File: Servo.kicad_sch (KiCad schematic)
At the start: 80 parts, among them J2 Conn_01x03_Pin, J3 Conn_01x03_Pin, J31 Conn_01x03_Pin, J32 Conn_01x03_Pin, J33 Conn_01x03_Pin, J34 Conn_01x03_Pin, J35 Conn_01x03_Pin, J36 Conn_01x03_Pin, J37 Conn_01x03_Pin, J38 Conn_01x03_Pin, J4 Conn_01x03_Pin, J5 Conn_01x03_Pin, J6 Conn_01x03_Pin, J7 Conn_01x03_Pin, J8 Conn_01x03_Pin, J9 Conn_01x03_Pin, Q19 2N7002, Q20 2N7002, Q21 2N7002, Q22 2N7002, Q23 2N7002, Q24 2N7002, Q25 2N7002, Q26 2N7002, Q27 2N7002, Q28 2N7002, Q29 2N7002, Q30 2N7002, Q31 2N7002, Q32 2N7002, Q33 2N7002, Q34 2N7002

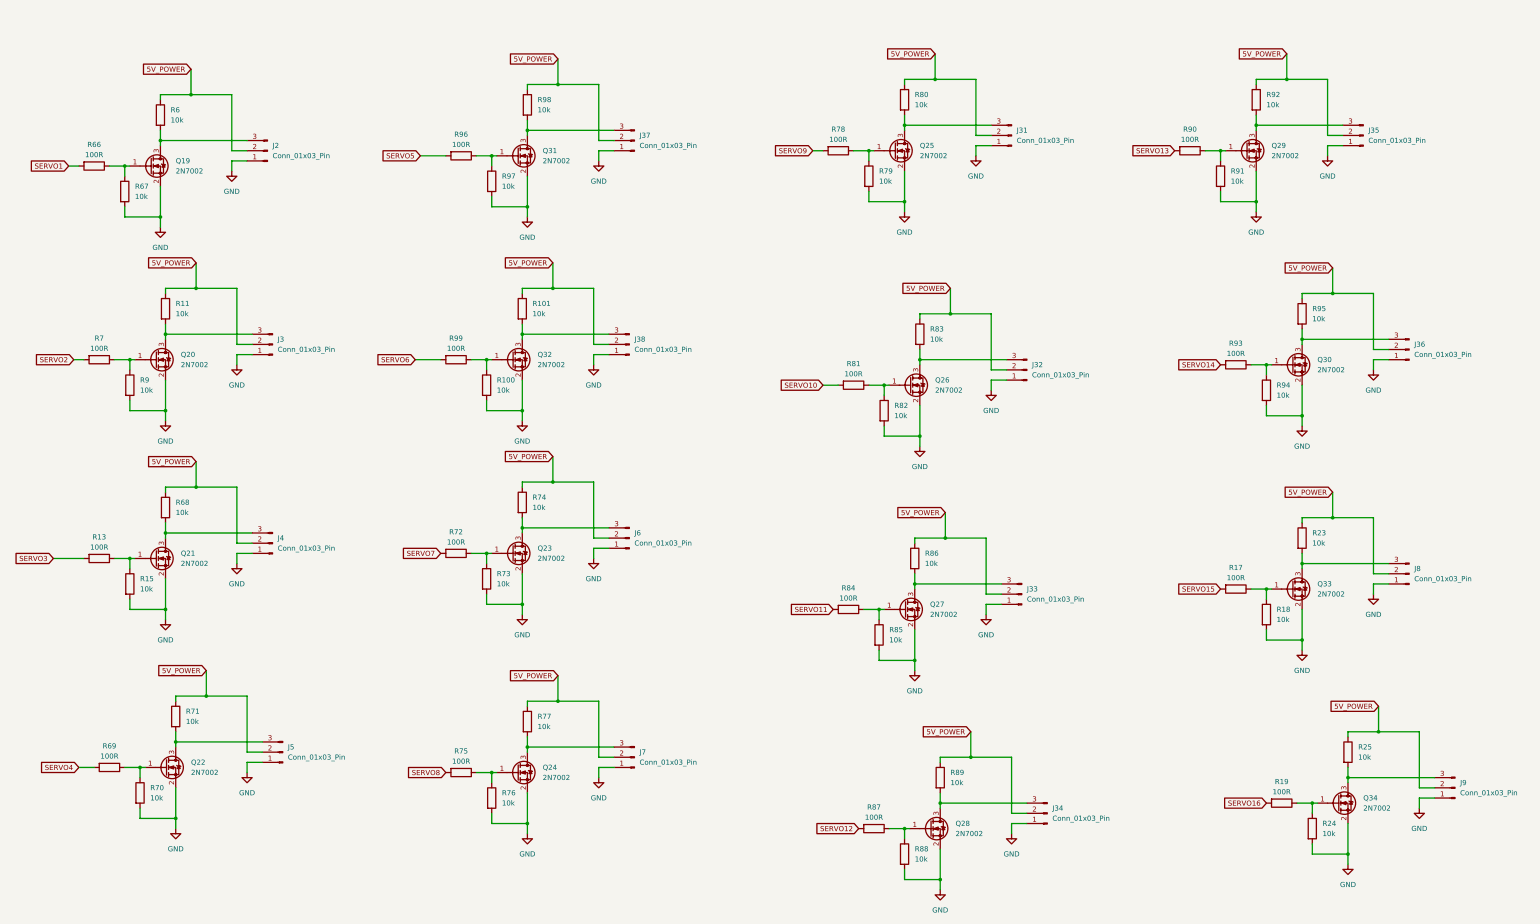
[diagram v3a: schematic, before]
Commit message: update schematic for feedback
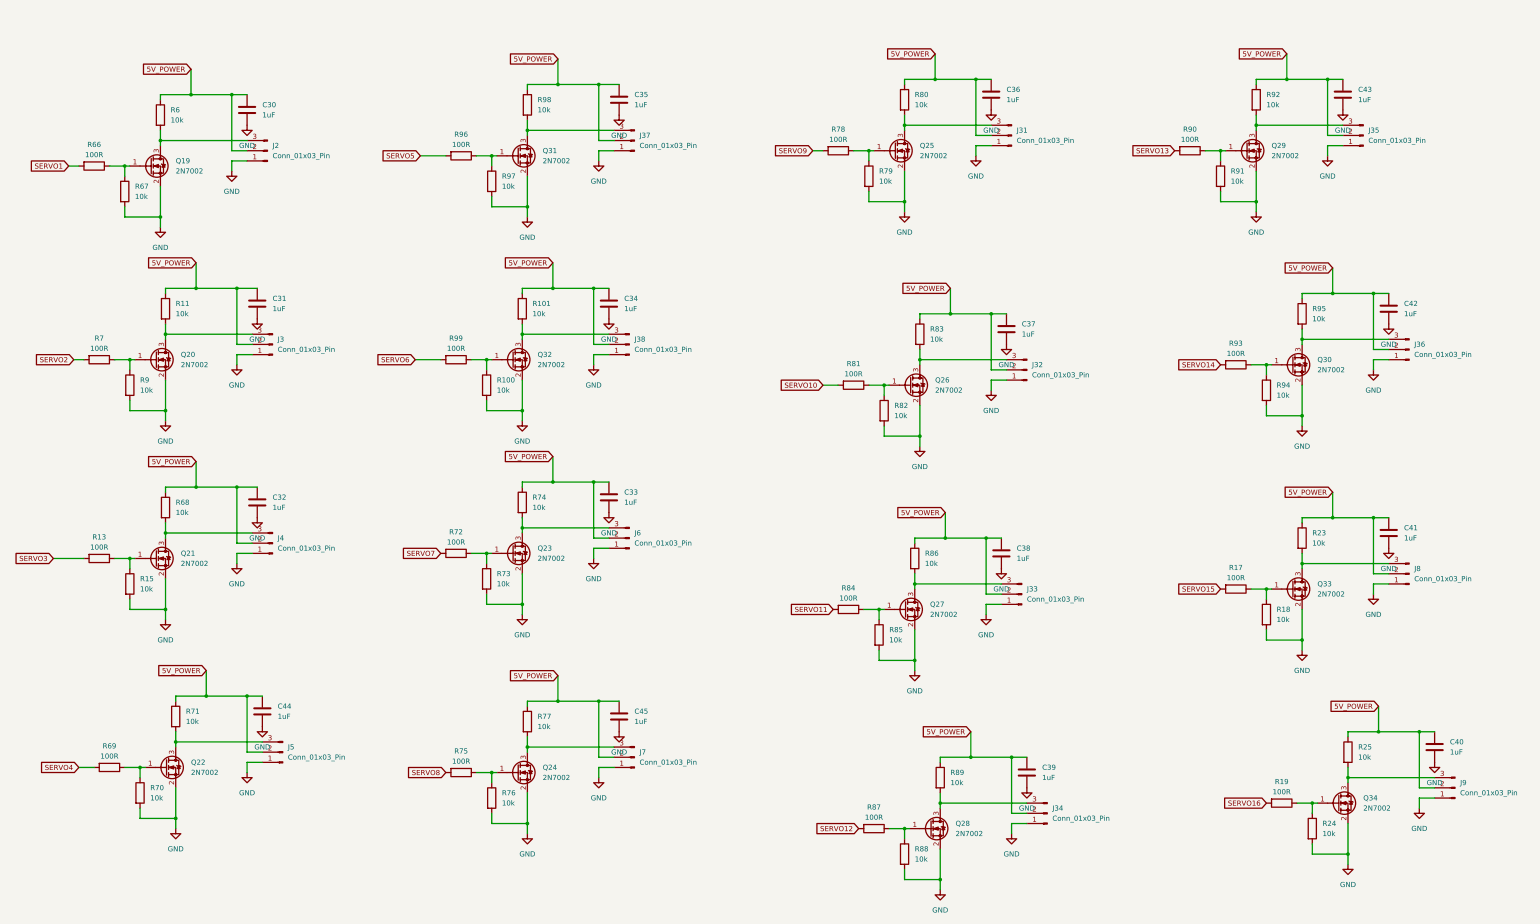
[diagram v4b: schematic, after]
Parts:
- added C30, C31, C32, C33, C34, C35, C36, C37, C38, C39, C40, C41, C42, C43, C44, C45: 1uF, Capacitor_SMD:C_0402_1005Metric, symbol Device:C
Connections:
- net 5V_POWER: now also C30.1, C31.1, C32.1, C33.1, C34.1, C35.1, C36.1, C37.1, C38.1, C39.1, C40.1, C41.1, C42.1, C43.1, C44.1, C45.1
- net GND: now also C30.2, C31.2, C32.2, C33.2, C34.2, C35.2, C36.2, C37.2, C38.2, C39.2, C40.2, C41.2, C42.2, C43.2, C44.2, C45.2

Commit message: update schematic
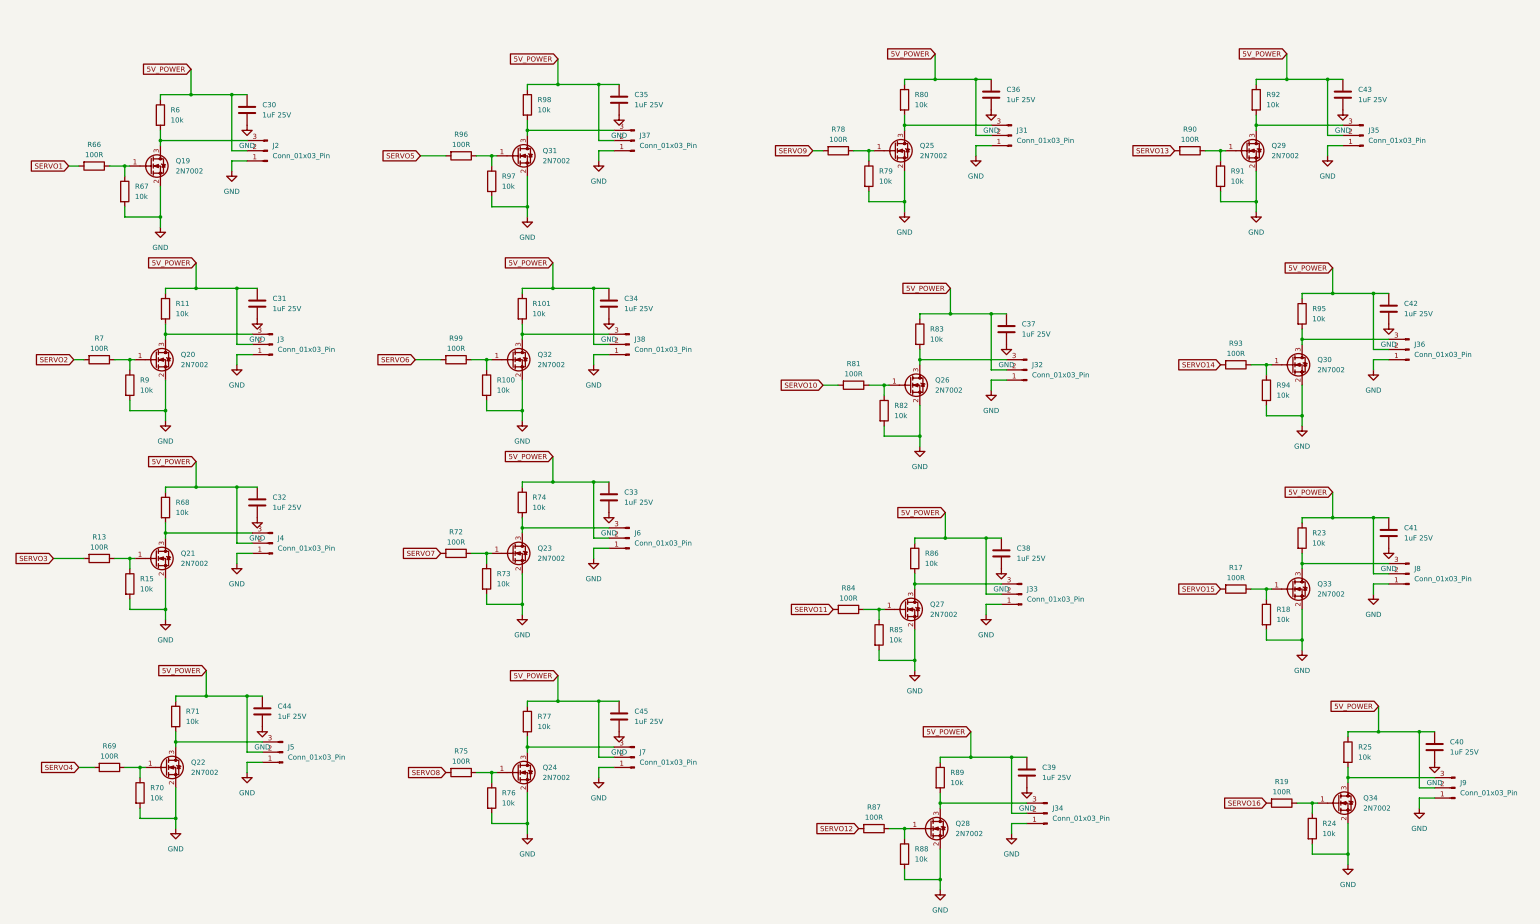
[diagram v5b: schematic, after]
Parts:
- C30, C31, C32, C33, C34, C35, C36, C37, C38, C39, C40, C41, C42, C43, C44, C45: value 1uF -> 1uF 25V
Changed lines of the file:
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@@
 			)
 		)
-		(property "Value" "1uF"
+		(property "Value" "1uF 25V"
 			(at 273.05 100.3299 0)
 			(effects
@@
 			)
 		)
-		(property "Value" "1uF"
+		(property "Value" "1uF 25V"
 			(at 173.99 142.2399 0)
 			(effects
@@
 			)
 		)
-		(property "Value" "1uF"
+		(property "Value" "1uF 25V"
 			(at 368.3 95.2499 0)
 			(effects
@@
 			)
 		)
-		(property "Value" "1uF"
+		(property "Value" "1uF 25V"
 			(at 176.53 43.1799 0)
 			(effects
@@
 			)
 		)
-		(property "Value" "1uF"
+		(property "Value" "1uF 25V"
 			(at 271.78 156.2099 0)
 			(effects
@@
 			)
 		)
-		(property "Value" "1uF"
+		(property "Value" "1uF 25V"
 			(at 87.63 195.5799 0)
 			(effects
@@
 			)
 		)
-		(property "Value" "1uF"
+		(property "Value" "1uF 25V"
 			(at 83.82 45.7199 0)
 			(effects
@@
 			)
 		)
-		(property "Value" "1uF"
+		(property "Value" "1uF 25V"
 			(at 278.13 210.8199 0)
 			(effects
@@
 			)
 		)
-		(property "Value" "1uF"
+		(property "Value" "1uF 25V"
 			(at 379.73 204.4699 0)
 			(effects
@@
 			)
 		)
-		(property "Value" "1uF"
+		(property "Value" "1uF 25V"
 			(at 356.87 41.9099 0)
 			(effects
@@
 			)
 		)
-		(property "Value" "1uF"
+		(property "Value" "1uF 25V"
 			(at 173.99 93.9799 0)
 			(effects
@@
 			)
 		)
-		(property "Value" "1uF"
+		(property "Value" "1uF 25V"
 			(at 368.3 151.1299 0)
 			(effects
@@
 			)
 		)
-		(property "Value" "1uF"
+		(property "Value" "1uF 25V"
 			(at 86.36 93.9799 0)
 			(effects
@@
 			)
 		)
-		(property "Value" "1uF"
+		(property "Value" "1uF 25V"
 			(at 86.36 143.5099 0)
 			(effects
@@
 			)
 		)
-		(property "Value" "1uF"
+		(property "Value" "1uF 25V"
 			(at 269.24 41.9099 0)
 			(effects
@@
 			)
 		)
-		(property "Value" "1uF"
+		(property "Value" "1uF 25V"
 			(at 176.53 196.8499 0)
 			(effects

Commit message: routage v2 ok - en attente de relecture
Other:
- moved on the sheet: C30
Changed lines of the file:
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@@
 	(wire
 		(pts
-			(xy 76.2 40.64) (xy 80.01 40.64)
+			(xy 76.2 40.64) (xy 95.25 40.64)
 		)
 		(stroke
@@
 	(symbol
 		(lib_id "Device:C")
-		(at 80.01 44.45 0)
+		(at 95.25 44.45 0)
 		(unit 1)
 		(exclude_from_sim no)
@@
 		(fields_autoplaced yes)
 		(property "Reference" "C30"
-			(at 83.82 43.1799 0)
+			(at 99.06 43.1799 0)
 			(effects
 				(font
@@
 		)
 		(property "Value" "1uF 25V"
-			(at 83.82 45.7199 0)
+			(at 99.06 45.7199 0)
 			(effects
 				(font
@@
 		)
 		(property "Footprint" "Capacitor_SMD:C_0402_1005Metric"
-			(at 80.9752 48.26 0)
+			(at 96.2152 48.26 0)
 			(effects
 				(font
@@
 		)
 		(property "Datasheet" "~"
-			(at 80.01 44.45 0)
+			(at 95.25 44.45 0)
 			(effects
 				(font
@@
 		)
 		(property "Description" ""
-			(at 80.01 44.45 0)
+			(at 95.25 44.45 0)
 			(effects
 				(font
@@
 	(symbol
 		(lib_id "power:GND")
-		(at 80.01 48.26 0)
+		(at 95.25 48.26 0)
 		(unit 1)
 		(exclude_from_sim no)
@@
 		(fields_autoplaced yes)
 		(property "Reference" "#PWR0110"
-			(at 80.01 54.61 0)
+			(at 95.25 54.61 0)
 			(effects
 				(font
@@
 		)
 		(property "Value" "GND"
-			(at 80.01 53.34 0)
+			(at 95.25 53.34 0)
 			(effects
 				(font
@@
 		)
 		(property "Footprint" ""
-			(at 80.01 48.26 0)
+			(at 95.25 48.26 0)
 			(effects
 				(font
@@
 		)
 		(property "Datasheet" ""
-			(at 80.01 48.26 0)
+			(at 95.25 48.26 0)
 			(effects
 				(font
@@
 		)
 		(property "Description" "Power symbol creates a global label with name \"GND\" , ground"
-			(at 80.01 48.26 0)
+			(at 95.25 48.26 0)
 			(effects
 				(font

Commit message: update
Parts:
- J2, J3, J31, J32, J33, J34, J35, J36, J37, J38, J4, J5, J6, J7, J8, J9: now left out of the parts list
- Q19, Q20, Q21, Q22, Q23, Q24, Q25, Q26, Q27, Q28, Q29, Q30, Q31, Q32, Q33, Q34: LCSC (none) -> C8545
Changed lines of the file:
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@@
 			)
 		)
+		(property "LCSC" "C8545 "
+			(at 340.36 107.95 0)
+			(effects
+				(font
+					(size 1.27 1.27)
+				)
+				(hide yes)
+			)
+		)
 		(pin "1"
 		)
@@
 		(unit 1)
 		(exclude_from_sim no)
-		(in_bom yes)
+		(in_bom no)
 		(on_board yes)
 		(dnp no)
@@
 			)
 		)
+		(property "LCSC" "C8545 "
+			(at 245.11 113.03 0)
+			(effects
+				(font
+					(size 1.27 1.27)
+				)
+				(hide yes)
+			)
+		)
 		(pin "1"
 		)
@@
 		(unit 1)
 		(exclude_from_sim no)
-		(in_bom yes)
+		(in_bom no)
 		(on_board yes)
 		(dnp no)
@@
 		(unit 1)
 		(exclude_from_sim no)
-		(in_bom yes)
+		(in_bom no)
 		(on_board yes)
 		(dnp no)
@@
 		(unit 1)
 		(exclude_from_sim no)
-		(in_bom yes)
+		(in_bom no)
 		(on_board yes)
 		(dnp no)
@@
 			)
 		)
+		(property "LCSC" "C8545"
+			(at 57.15 106.68 0)
+			(effects
+				(font
+					(size 1.27 1.27)
+				)
+				(hide yes)
+			)
+		)
 		(pin "1"
 		)
@@
 			)
 		)
+		(property "LCSC" "C8545 "
+			(at 146.05 154.94 0)
+			(effects
+				(font
+					(size 1.27 1.27)
+				)
+				(hide yes)
+			)
+		)
 		(pin "1"
 		)
@@
 		(unit 1)
 		(exclude_from_sim no)
-		(in_bom yes)
+		(in_bom no)
 		(on_board yes)
 		(dnp no)
@@
 			)
 		)
+		(property "LCSC" "C8545 "
+			(at 351.79 217.17 0)
+			(effects
+				(font
+					(size 1.27 1.27)
+				)
+				(hide yes)
+			)
+		)
 		(pin "1"
 		)
@@
 		(unit 1)
 		(exclude_from_sim no)
-		(in_bom yes)
+		(in_bom no)
 		(on_board yes)
 		(dnp no)
@@
 		(unit 1)
 		(exclude_from_sim no)
-		(in_bom yes)
+		(in_bom no)
 		(on_board yes)
 		(dnp no)
@@
 			)
 		)
+		(property "LCSC" "C8545"
+			(at 57.15 156.21 0)
+			(effects
+				(font
+					(size 1.27 1.27)
+				)
+				(hide yes)
+			)
+		)
 		(pin "1"
 		)
@@
 			)
 		)
+		(property "LCSC" "C8545 "
+			(at 147.32 55.88 0)
+			(effects
+				(font
+					(size 1.27 1.27)
+				)
+				(hide yes)
+			)
+		)
 		(pin "1"
 		)
@@
 		(unit 1)
 		(exclude_from_sim no)
-		(in_bom yes)
+		(in_bom no)
 		(on_board yes)
 		(dnp no)
@@
 		(unit 1)
 		(exclude_from_sim no)
-		(in_bom yes)
+		(in_bom no)
 		(on_board yes)
 		(dnp no)
@@
 			)
 		)
+		(property "LCSC" "C8545 "
+			(at 146.05 106.68 0)
+			(effects
+				(font
+					(size 1.27 1.27)
+				)
+				(hide yes)
+			)
+		)
 		(pin "1"
 		)
@@
 			)
 		)
+		(property "LCSC" "C8545 "
+			(at 241.3 54.61 0)
+			(effects
+				(font
+					(size 1.27 1.27)
+				)
+				(hide yes)
+			)
+		)
 		(pin "1"
 		)
@@
 			)
 		)
+		(property "LCSC" "C8545 "
+			(at 243.84 168.91 0)
+			(effects
+				(font
+					(size 1.27 1.27)
+				)
+				(hide yes)
+			)
+		)
 		(pin "1"
 		)
@@
 		(unit 1)
 		(exclude_from_sim no)
-		(in_bom yes)
+		(in_bom no)
 		(on_board yes)
 		(dnp no)
@@
 			)
 		)
+		(property "LCSC" "C8545"
+			(at 59.69 208.28 0)
+			(effects
+				(font
+					(size 1.27 1.27)
+				)
+				(hide yes)
+			)
+		)
 		(pin "1"
 		)
@@
 		(unit 1)
 		(exclude_from_sim no)
-		(in_bom yes)
+		(in_bom no)
 		(on_board yes)
 		(dnp no)
@@
 		(unit 1)
 		(exclude_from_sim no)
-		(in_bom yes)
+		(in_bom no)
 		(on_board yes)
 		(dnp no)
@@
 		(unit 1)
 		(exclude_from_sim no)
-		(in_bom yes)
+		(in_bom no)
 		(on_board yes)
 		(dnp no)
@@
 			)
 		)
+		(property "LCSC" "C8545 "
+			(at 328.93 54.61 0)
+			(effects
+				(font
+					(size 1.27 1.27)
+				)
+				(hide yes)
+			)
+		)
 		(pin "1"
 		)
@@
 			)
 		)
+		(property "LCSC" "C8545 "
+			(at 250.19 223.52 0)
+			(effects
+				(font
+					(size 1.27 1.27)
+				)
+				(hide yes)
+			)
+		)
 		(pin "1"
 		)
@@
 		(unit 1)
 		(exclude_from_sim no)
-		(in_bom yes)
+		(in_bom no)
 		(on_board yes)
 		(dnp no)
@@
 		(unit 1)
 		(exclude_from_sim no)
-		(in_bom yes)
+		(in_bom no)
 		(on_board yes)
 		(dnp no)
@@
 			)
 		)
+		(property "LCSC" " C8545 "
+			(at 147.32 209.55 0)
+			(effects
+				(font
+					(size 1.27 1.27)
+				)
+				(hide yes)
+			)
+		)
 		(pin "1"
 		)
@@
 		(unit 1)
 		(exclude_from_sim no)
-		(in_bom yes)
+		(in_bom no)
 		(on_board yes)
 		(dnp no)
@@
 			)
 		)
+		(property "LCSC" "C8545 "
+			(at 340.36 163.83 0)
+			(effects
+				(font
+					(size 1.27 1.27)
+				)
+				(hide yes)
+			)
+		)
 		(pin "1"
 		)
@@
 			(at 55.88 58.42 0)
 			(effects
+				(font
+					(size 1.27 1.27)
+				)
+				(hide yes)
+			)
+		)
+		(property "LCSC" " C8545"
+			(at 55.88 58.42 0)
+			(effects
